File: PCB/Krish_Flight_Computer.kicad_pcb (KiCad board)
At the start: 2 copper layers, 47.1 x 65.4 mm, 35 parts, among them J1 I2C, J3 UART, J4 SW, J5 BAT, U1 MS5611-01BA, U2 MMC5633NJL, U3 BMI088

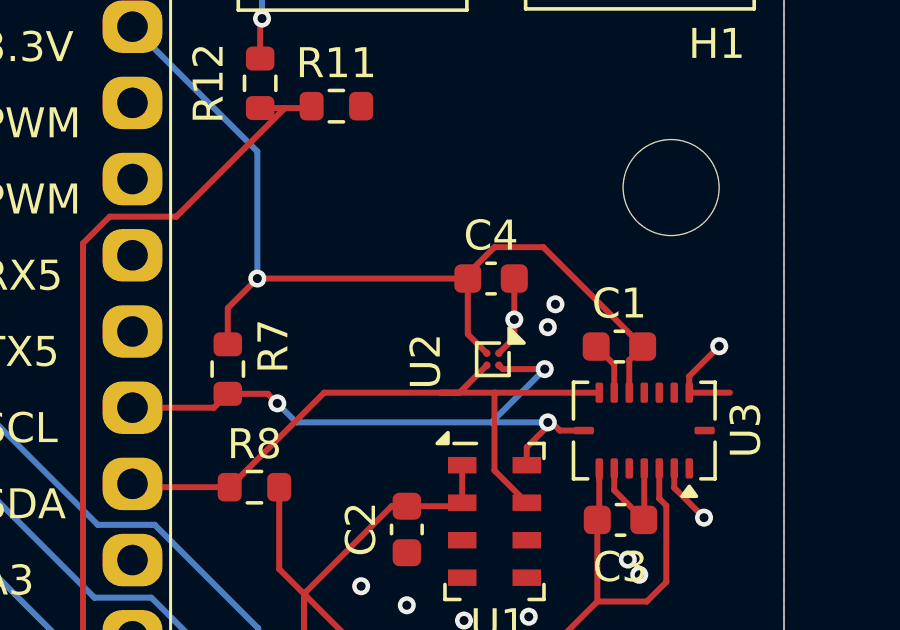
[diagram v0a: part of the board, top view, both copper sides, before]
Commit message: removed MMC5603
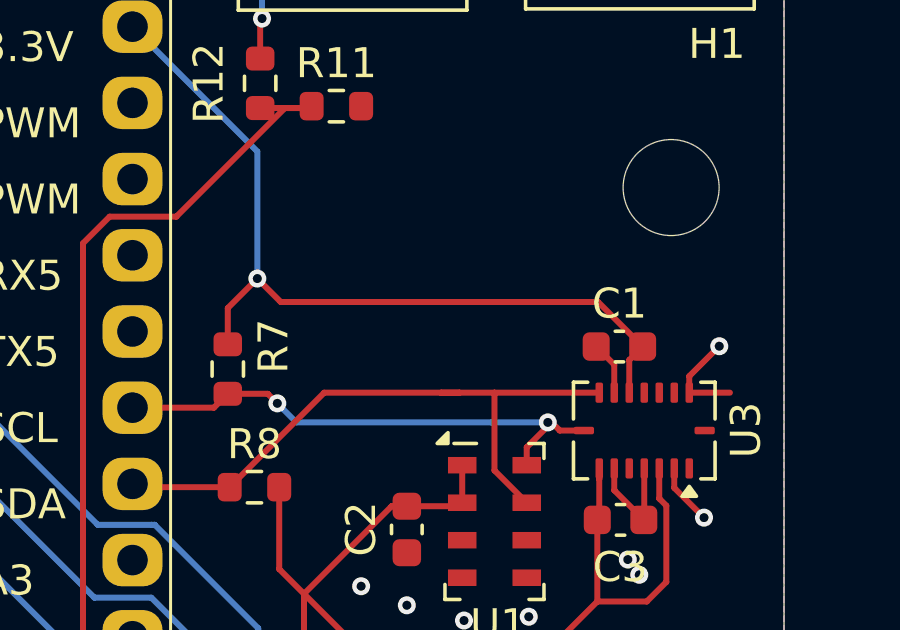
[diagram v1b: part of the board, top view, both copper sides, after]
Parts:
- removed C4: 100 nF, Capacitor_SMD:C_0603_1608Metric
- removed U2: MMC5633NJL, Package_BGA:WLP-4_0.86x0.86mm_P0.4mm
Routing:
- net SCLK: track 21.5 -> 17.5 mm, vias 3 -> 2
- net +3V3: track 144.3 -> 140.7 mm
- net GND: track 13.7 -> 11.0 mm, vias 11 -> 8
- net SDA: track 22.9 -> 21.6 mm
